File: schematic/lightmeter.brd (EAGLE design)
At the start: 27.9 x 52.6 mm, 80 parts, among them IC2 MCP73831/OT, J1 AVR_SPI_PRG_6NS, Q1 NCHANNELMOSFET, Q10 PCHANNELMOSFET, Q11 NCHANNELMOSFET, Q12 NCHANNELMOSFET, Q13 NCHANNELMOSFET, Q14 NCHANNELMOSFET, Q16 NCHANNELMOSFET, Q2 PCHANNELMOSFET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

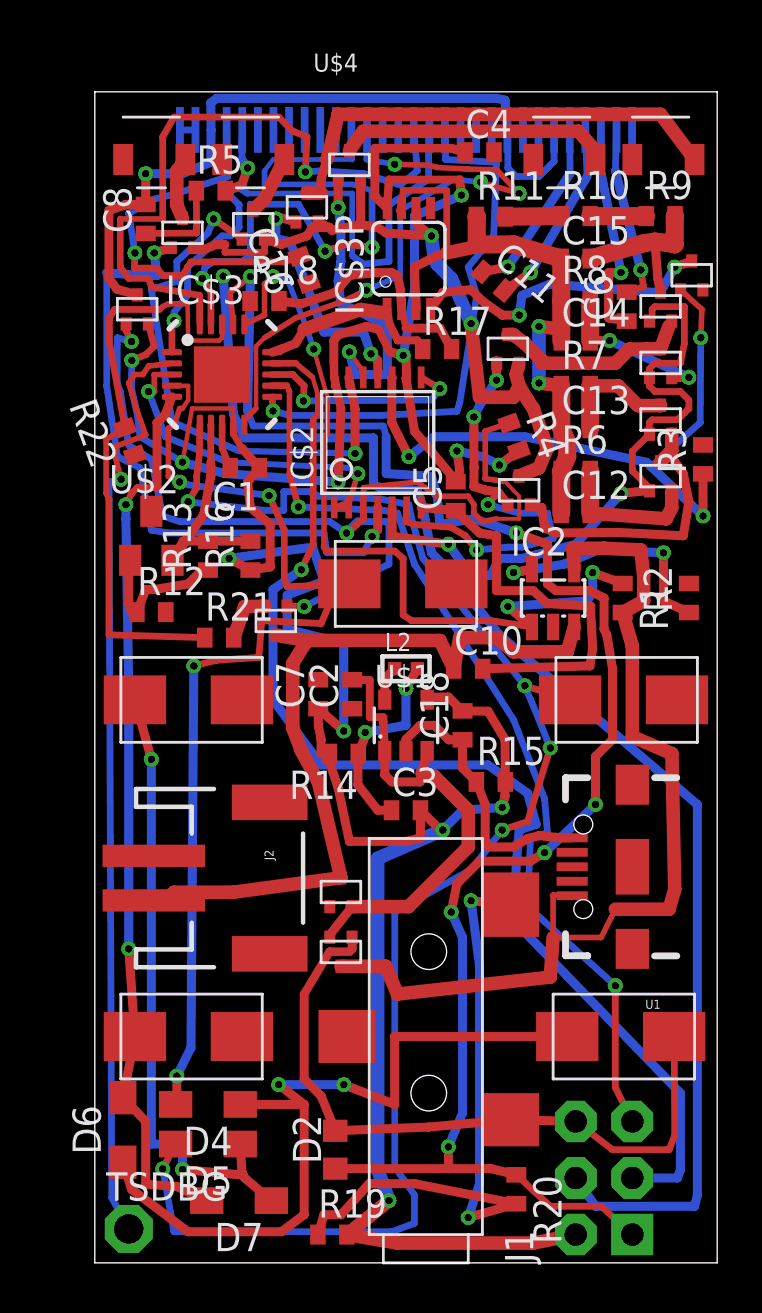
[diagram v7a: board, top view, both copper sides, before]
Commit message: More progess on fixing design rules errors
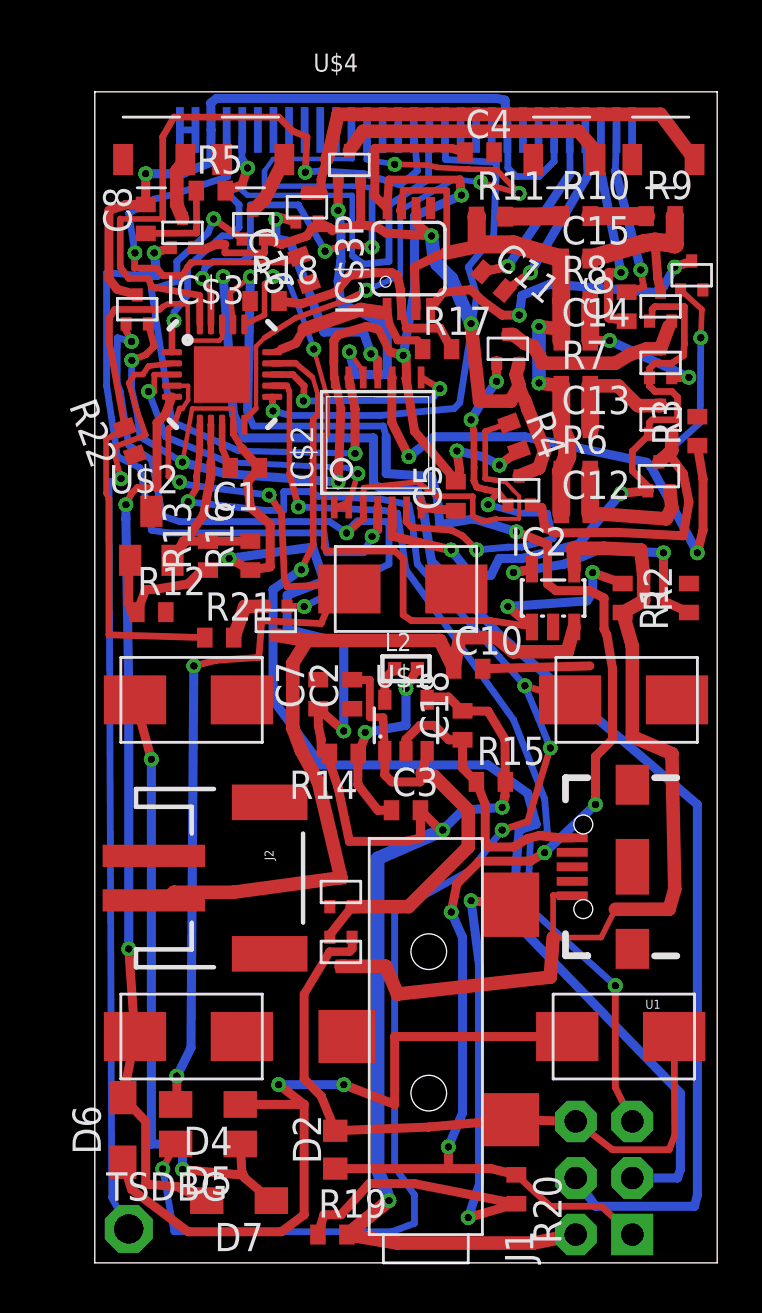
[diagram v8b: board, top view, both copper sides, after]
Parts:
- moved R3 1.30 mm to (25.8, 37.3)
- moved S2 0.23 mm to (12.7, 30.3)
- moved Q4 0.08 mm to (24.1, 35.6)
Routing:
- net GND: track 69.1 -> 57.2 mm
- net OAPWR: track 29.6 -> 33.7 mm
- net STG$1: track 30.3 -> 29.6 mm
